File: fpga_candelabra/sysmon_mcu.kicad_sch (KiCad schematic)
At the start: 38 parts, among them J1 TYPE-C-31-M-12, J2 DNP/MCU_DEBUG, SW1 TS-1187A, U17 W25Q128JVS, U21 PCA9306DC, U8 RP2040, Y1 12MHz 20pF

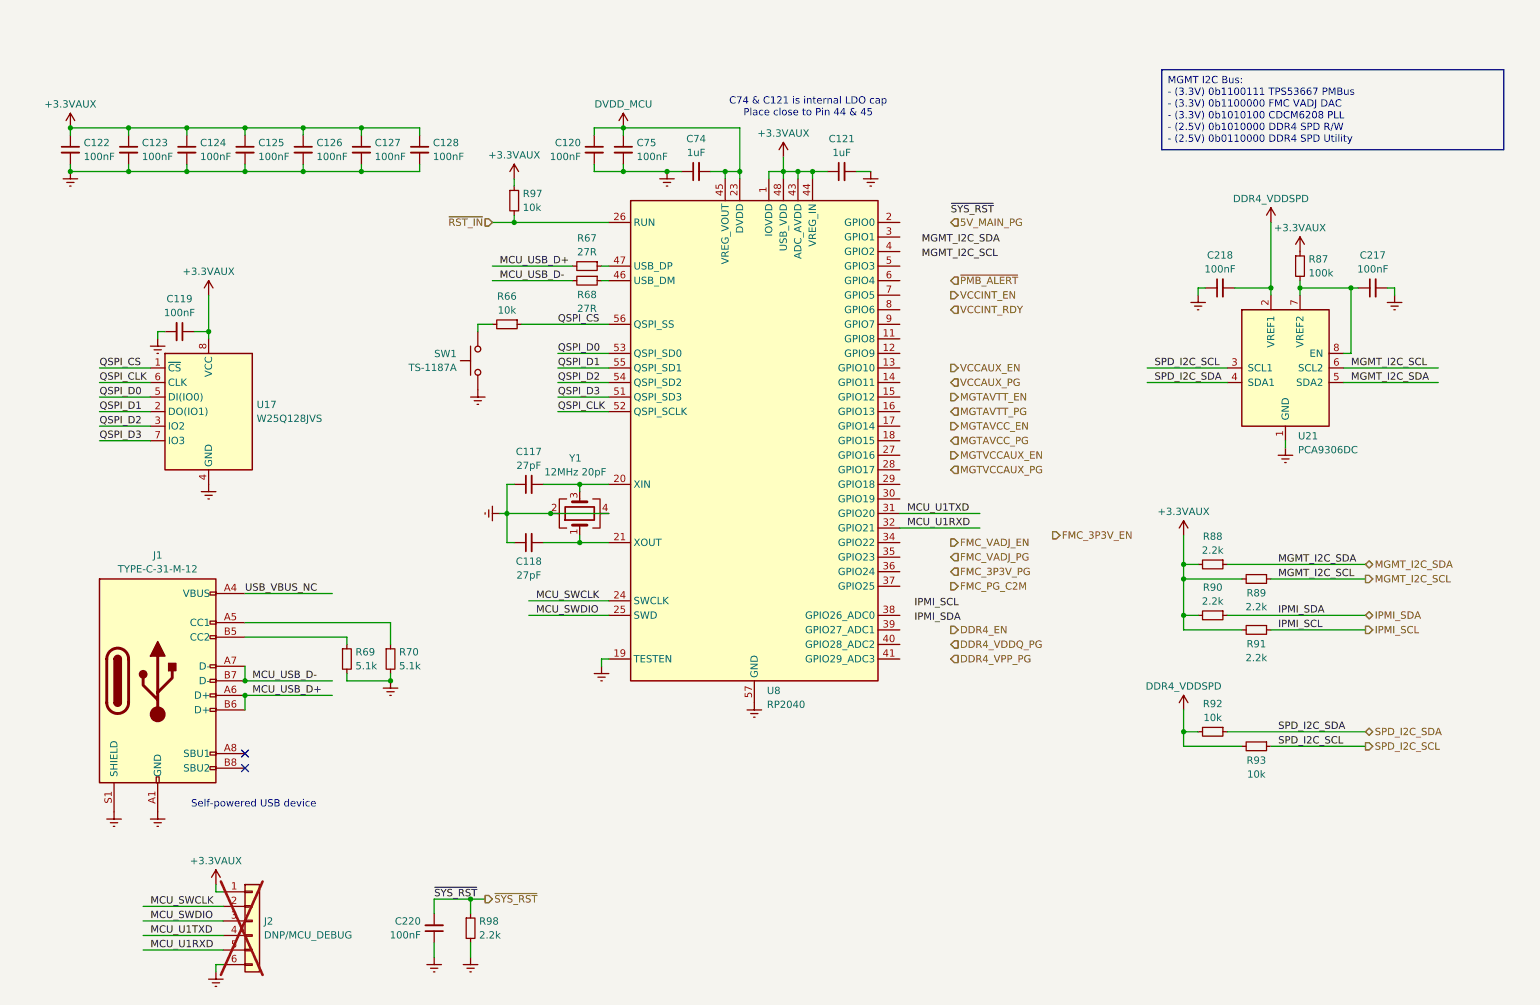
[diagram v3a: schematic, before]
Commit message: fpga_candelabra: sch & layout v0.5, pass basic ERC & DRC
Signed-off-by: Yichuan Gao <gaoyichuan000@gmail.com>
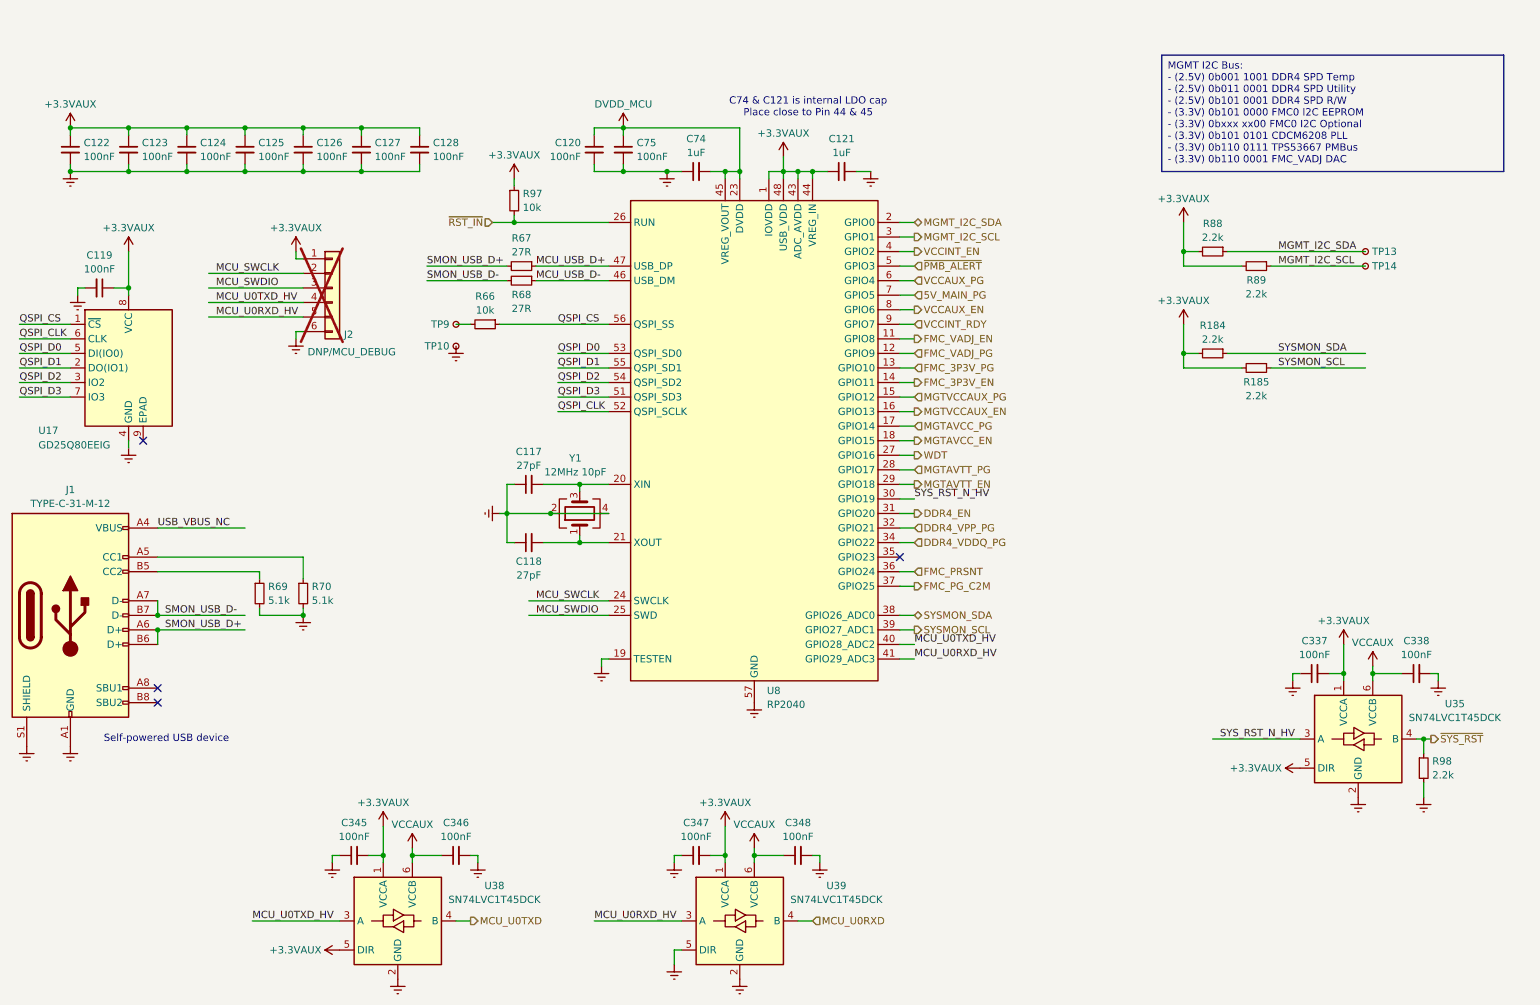
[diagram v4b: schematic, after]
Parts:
- removed C217, C218, C220: 100nF, Capacitor_SMD:C_0402_1005Metric, symbol Device:C_Small
- removed R87: 100k, Resistor_SMD:R_0402_1005Metric, symbol Device:R_Small
- removed R90, R91: 2.2k, Resistor_SMD:R_0402_1005Metric, symbol Device:R_Small
- removed R92, R93: 10k, Resistor_SMD:R_0402_1005Metric, symbol Device:R_Small
- removed SW1: TS-1187A, Button_Switch_SMD:SW_Push_1P1T_XKB_TS-1187A, symbol Switch:SW_Push
- removed U21: PCA9306DC, Package_SO:VSSOP-8_2.3x2mm_P0.5mm, symbol Interface:PCA9306DC
- added C337, C338, C345, C346, C347, C348: 100nF, Capacitor_SMD:C_0402_1005Metric, symbol Device:C_Small
- added R184, R185: 2.2k, Resistor_SMD:R_0402_1005Metric, symbol Device:R_Small
- added TP10, TP9: TestPoint_Small, TestPoint:TestPoint_THTPad_D1.0mm_Drill0.5mm, symbol Connector:TestPoint_Small
- added TP13, TP14: TestPoint_Small, TestPoint:TestPoint_Pad_D1.0mm, symbol Connector:TestPoint_Small
- added U35, U38, U39: SN74LVC1T45DCK, Package_TO_SOT_SMD:SOT-363_SC-70-6, symbol Logic_LevelTranslator:SN74LVC1T45DCK
- J2: now left out of the parts list
- U17: value W25Q128JVS -> GD25Q80EEIG; footprint Package_SO:SOIC-8_5.23x5.23mm_P1.27mm -> Package_SON:Winbond_USON-8-1EP_3x2mm_P0.5mm_EP0.2x1.6mm; symbol Memory_Flash:W25Q128JVS -> CHIPSAlliance_Memory_Flash:GD25Q80EEIG
- Y1: value 12MHz 20pF -> 12MHz 10pF; footprint Crystal:Crystal_SMD_3225-4Pin_3.2x2.5mm -> Crystal:Crystal_SMD_2520-4Pin_2.5x2.0mm; LCSC Part C9002 -> C2896601
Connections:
- net +3.3VAUX: now also C337.2, C345.2, C347.2, R184.2, R185.2, U35.1 (VCCA), U35.5 (DIR), U38.1 (VCCA), U38.5 (DIR), U39.1 (VCCA)
- net 5V_MAIN_PG: now also U8.7 (GPIO5)
- net DDR4_EN: now also U8.31 (GPIO20)
- net DDR4_VDDQ_PG: now also U8.34 (GPIO22)
- net DDR4_VPP_PG: now also U8.32 (GPIO21)
- net Earth: now also C337.1, C338.2, C345.1, C346.2, C347.1, C348.2, TP10.1, U35.2 (GND), U38.2 (GND), U39.2 (GND), U39.5 (DIR)
- net FMC_3P3V_EN: now also U8.14 (GPIO11)
- net FMC_3P3V_PG: now also U8.13 (GPIO10)
- net FMC_PG_C2M: now also U8.37 (GPIO25)
- net FMC_VADJ_EN: now also U8.11 (GPIO8)
- net FMC_VADJ_PG: now also U8.12 (GPIO9)
- net MCU_USB_D+: now also R67.1, U8.47 (USB_DP); no longer J1.A6 (D+), J1.B6 (D+), R67.2
- net MCU_USB_D-: now also R68.1, U8.46 (USB_DM); no longer J1.A7 (D-), J1.B7 (D-), R68.2
- net MGMT_I2C_SCL: now also U8.3 (GPIO1), TP14.1
- net MGMT_I2C_SDA: now also U8.2 (GPIO0), TP13.1
- net MGTAVCC_EN: now also U8.18 (GPIO15)
- net MGTAVCC_PG: now also U8.17 (GPIO14)
- net MGTAVTT_EN: now also U8.29 (GPIO18)
- net MGTAVTT_PG: now also U8.28 (GPIO17)
- net MGTVCCAUX_EN: now also U8.16 (GPIO13)
- net MGTVCCAUX_PG: now also U8.15 (GPIO12)
- net VCCAUX_EN: now also U8.8 (GPIO6)
- net VCCAUX_PG: now also U8.6 (GPIO4)
- net VCCINT_EN: now also U8.4 (GPIO2)
- net VCCINT_RDY: now also U8.9 (GPIO7)
- net ~{PMB_ALERT}: now also U8.5 (GPIO3)
- net ~{SYS_RST}: now also U35.4 (B)
- net at R66.2: now also TP9.1
- net WDT: now reaches U8.27 (GPIO16)
- net SYS_RST_N_HV: now reaches U8.30 (GPIO19)
- net SYS_RST_N_HV: now also U35.3 (A)
- net FMC_PRSNT: now reaches U8.36 (GPIO24)
- net SYSMON_SDA: now reaches U8.38 (GPIO26_ADC0)
- net SYSMON_SDA: now also R184.1
- net SYSMON_SCL: now reaches U8.39 (GPIO27_ADC1)
- net SYSMON_SCL: now also R185.1
- net MCU_U0TXD_HV: now reaches U8.40 (GPIO28_ADC2)
- net MCU_U0TXD_HV: now also J2.4 (Pin_4), U38.3 (A)
- net MCU_U0RXD_HV: now reaches U8.41 (GPIO29_ADC3)
- net MCU_U0RXD_HV: now also J2.5 (Pin_5), U39.3 (A)
- removed net MCU_U1RXD: J2.5 (Pin_5), U8.32 (GPIO21)
- removed net MCU_U1TXD: J2.4 (Pin_4), U8.31 (GPIO20)
- new net MCU_U0RXD: U39.4 (B)
- new net MCU_U0TXD: U38.4 (B)
- new net SMON_USB_D+: J1.A6 (D+), J1.B6 (D+), R67.2
- new net SMON_USB_D-: J1.A7 (D-), J1.B7 (D-), R68.2
- new net VCCAUX: C338.1, C346.1, C348.1, U35.6 (VCCB), U38.6 (VCCB), U39.6 (VCCB)
- no-connect marks 2 -> 4
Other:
- moved on the sheet: C119, J1, J2, R66, R67, R68, R69, R70, R88, R89

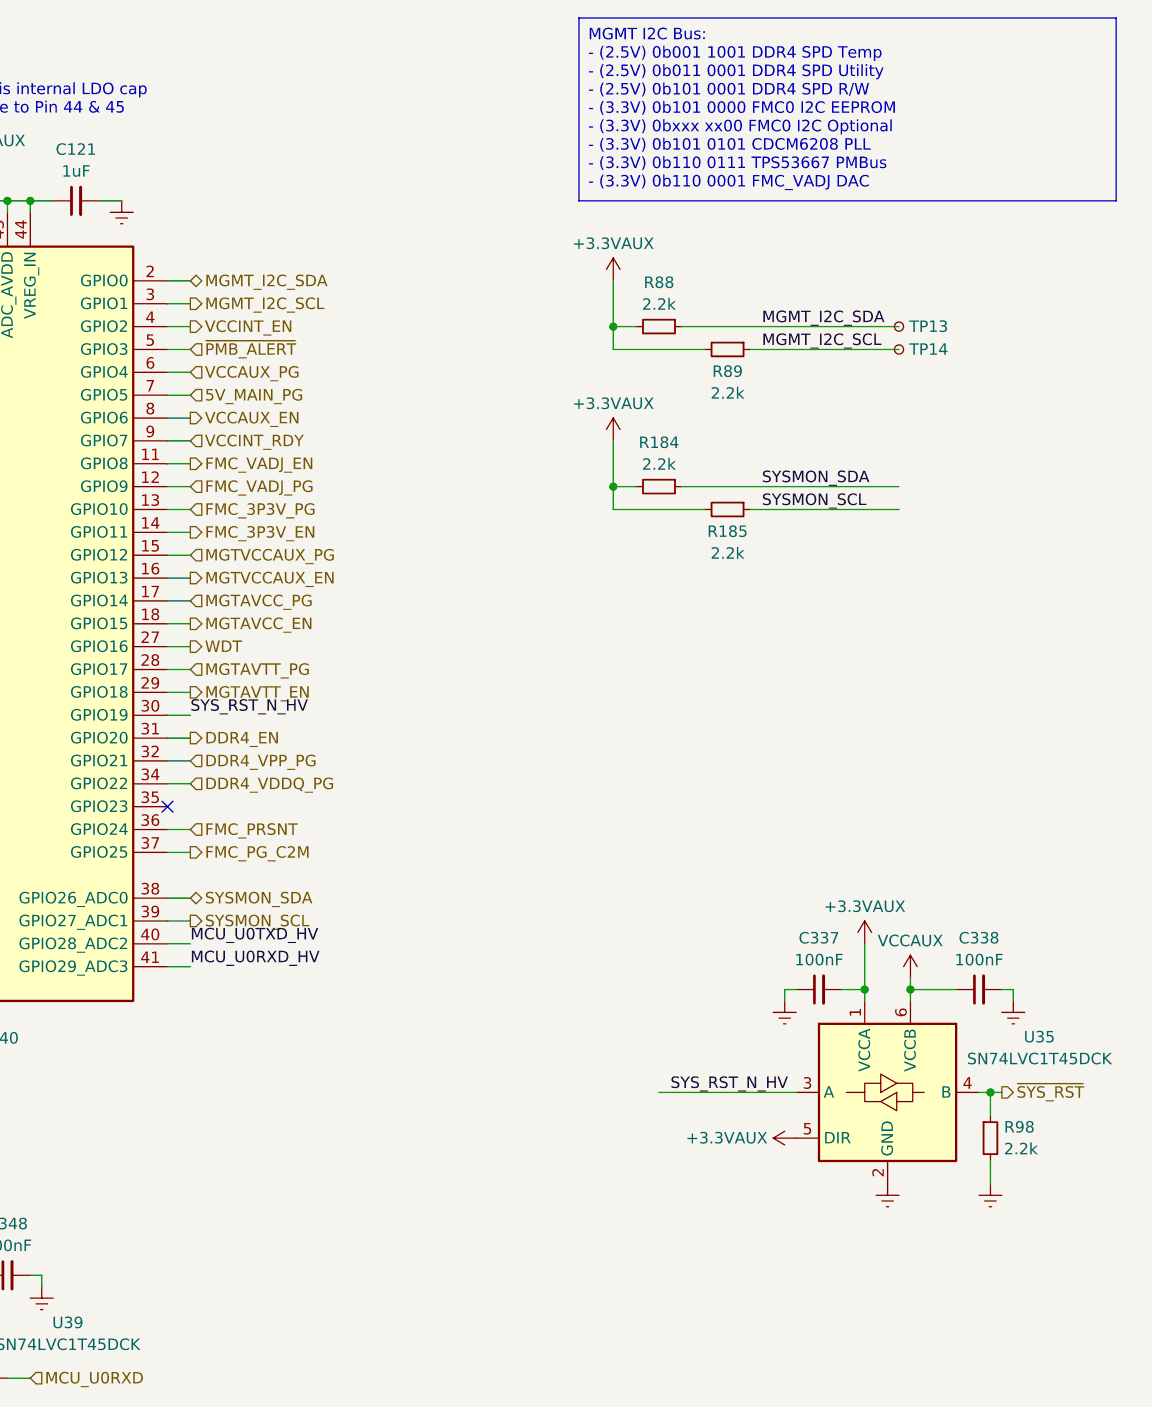
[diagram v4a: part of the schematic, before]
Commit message: fpga_candelabra: first rev fixes - fix vccint power stage FCCM mode - add ddr4 vref decoupling cap - refactor status LEDs - minor layout changes
Signed-off-by: Yichuan Gao <gaoyichuan000@gmail.com>
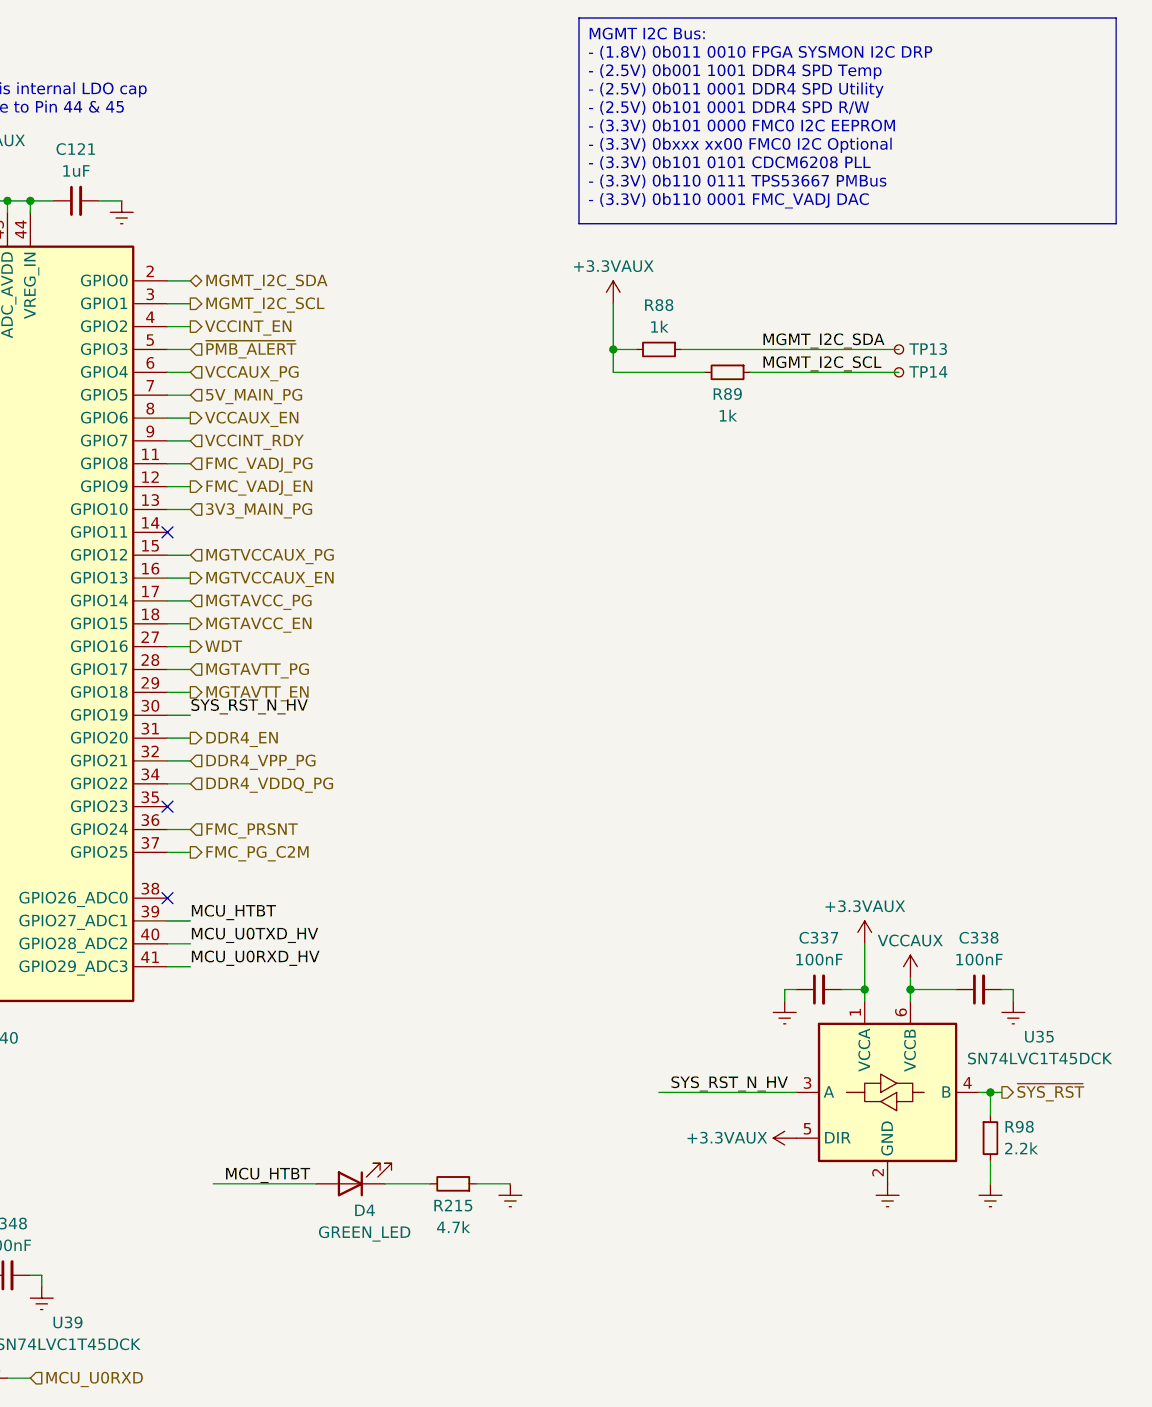
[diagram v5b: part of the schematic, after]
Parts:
- removed R184, R185: 2.2k, Resistor_SMD:R_0402_1005Metric, symbol Device:R_Small
- added D4: GREEN_LED, LED_SMD:LED_0603_1608Metric, symbol Device:LED
- added R215: 4.7k, Resistor_SMD:R_0402_1005Metric, symbol Device:R_Small
- R88, R89: value 2.2k -> 1k
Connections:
- net Earth: now also R215.1
- net FMC_VADJ_EN: now also U8.12 (GPIO9); no longer U8.11 (GPIO8)
- net FMC_VADJ_PG: now also U8.11 (GPIO8); no longer U8.12 (GPIO9)
- net FMC_3P3V_EN: no longer names the net of U8.14 (GPIO11)
- net FMC_3P3V_PG renamed 3V3_MAIN_PG
- net SYSMON_SCL renamed MCU_HTBT
- net MCU_HTBT: now also D4.2 (A)
- net SYSMON_SDA: no longer names the net of U8.38 (GPIO26_ADC0)
- new net: D4.1 (K), R215.2
- no-connect marks 4 -> 6
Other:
- moved on the sheet: R88, R89, TP13, TP14
